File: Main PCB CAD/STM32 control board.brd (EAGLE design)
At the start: 130 x 100 mm, 118 parts, among them J1 PJ-063BH, J10 S3B-PH, J11 S3B-PH, J12 S3B-PH, J13 S3B-PH, J14 S6B-PH, J15 DG301-4P, J2 S3B-PH, J3 S4B-PH, J4 S6B-PH, J5 S3B-PH, J6 S10B-PH, J7 S10B-PH, J8 S10B-PH, J9 S10B-PH, SW1 B3F-4055, SW2 B3F-4055, SW3 B3F-4055, SW4 B3F-4055, SW5 B3F-4055, U1 STM32G474, U2 TPS7A19, U3 REF3330, U4 REF3318, U5 ICM_20600, U6 DRV8701VIA, U8 L2293Q, X1 CSTNE

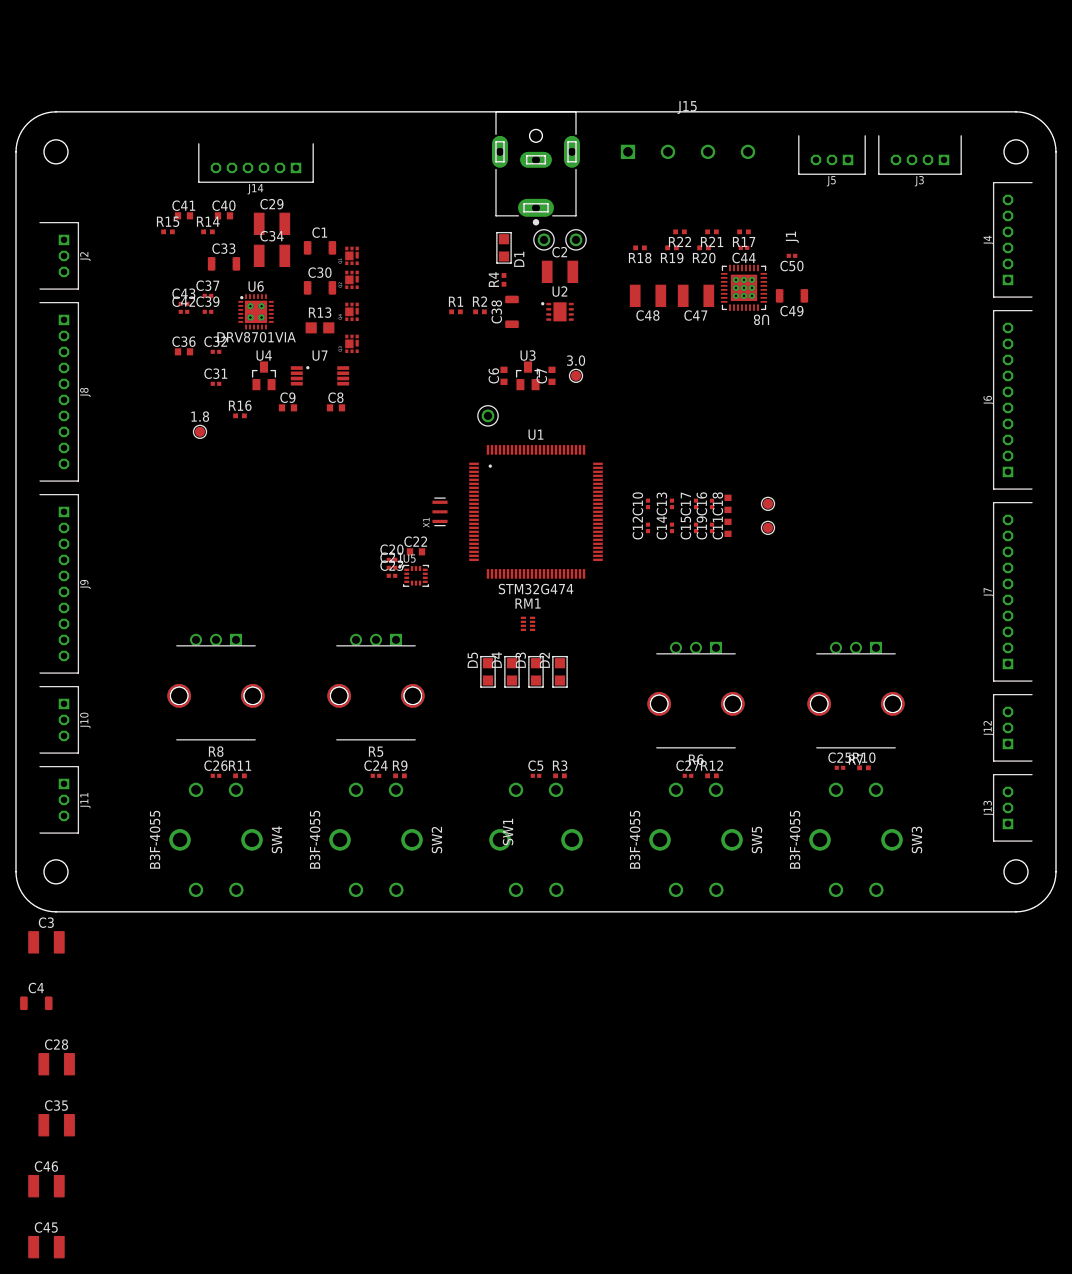
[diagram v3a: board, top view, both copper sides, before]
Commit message: components placement for review
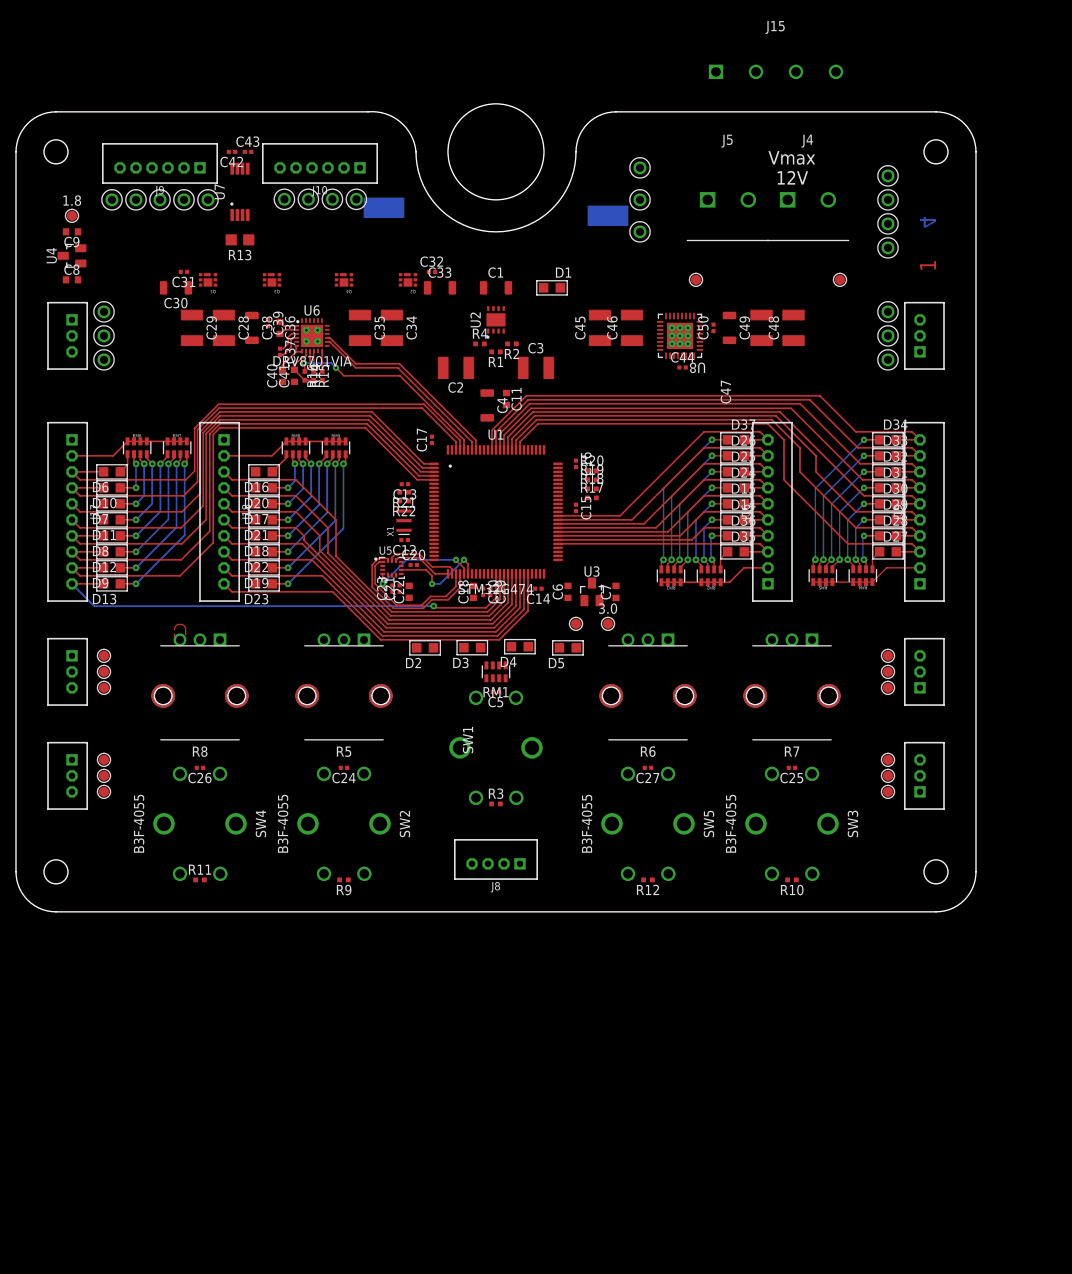
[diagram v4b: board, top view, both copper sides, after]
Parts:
- removed J1: PJ-063BH, commonly used connectors:CUI_PJ-063BH
- removed J11, J12, J13, J2: S3B-PH, con-jst-ph:S3B-PH-K
- removed J14: S6B-PH, con-jst-ph:S6B-PH-K
- removed J3: S4B-PH, con-jst-ph:S4B-PH-K
- added D10, D11, D12, D13, D14, D15, D16, D17, D18, D19, D20, D21, D22, D23, D24, D25, D26, D27, D28, D29, D30, D31, D32, D33, D34, D35, D36, D37, D6, D7, D8, D9: Blue, Semiconductor_devices:LED-0805
- added GND_, TP12, TP13, TP14, TP15, TP16, TP17, TP37, TP38, TP6, TP7, TP8, TP9: (no value), testing:TP1.27MM_MASK_SILKSCREEN
- added J16, J17, J18, J19: B10B-PH, con-jst-ph:B10B-PH-K
- added J20, J21, J22, J23: B3B-PH, con-jst-ph:B3B-PH-K
- added NEG, POS: (no value), testing:SMD_PAD
- added RM2, RM3, RM4, RM5, RM6, RM7, RM8, RM9: RES_ARRAY0603, Resistors:0603-ARC
- added TP18, TP19, TP20, TP21, TP22, TP23, TP24, TP25, TP26, TP27, TP28, TP29, TP30, TP31, TP32, TP33, TP34, TP35, TP36: (no value), testing:TEST_RING
- J10: value S3B-PH -> B6B-PH; device con-jst-ph:S3B-PH-K -> con-jst-ph:B6B-PH-K
- J4: value S6B-PH -> PC_1733570; device con-jst-ph:S6B-PH-K -> Terminal blocks:PC_1733570
- J5: value S3B-PH -> PC_1733570; device con-jst-ph:S3B-PH-K -> Terminal blocks:PC_1733570
- J6, J7: value S10B-PH -> B3B-PH; device con-jst-ph:S10B-PH-K -> con-jst-ph:B3B-PH-K
- J8: value S10B-PH -> B4B-PH; device con-jst-ph:S10B-PH-K -> con-jst-ph:B4B-PH-K
- J9: value S10B-PH -> B6B-PH; device con-jst-ph:S10B-PH-K -> con-jst-ph:B6B-PH-K
- RM1: value RES_ARRAY0402_YAGEO -> RES_ARRAY0603; device Resistors:0402-ARC -> Resistors:0603-ARC
- moved C45 134.1 mm to (73.0, 73.0), turned to 90 degrees
- moved C46 129.9 mm to (77.0, 73.0), turned to 90 degrees
- moved J7 121.3 mm to (7.00, 72.0), turned to 270 degrees
- moved C35 106.6 mm to (43.0, 73.0), turned to 270 degrees
- moved C28 94.4 mm to (26.0, 73.0), turned to 270 degrees
- moved C3 94.3 mm to (65.0, 68.0)
- moved C4 93.6 mm to (58.9, 63.3), turned to 270 degrees
- moved J8 80.0 mm to (60.0, 6.00), turned to 180 degrees
- moved J10 76.1 mm to (38.0, 93.0), turned to 180 degrees
- moved J9 53.4 mm to (18.0, 93.0), turned to 180 degrees
- moved R21 50.4 mm to (48.5, 52.5)
- moved R22 48.2 mm to (48.5, 51.4)
- moved R17 38.3 mm to (72.0, 51.7), turned to 0 degrees
- moved C8 36.7 mm to (7.00, 79.0)
- moved C9 34.8 mm to (7.00, 85.0), turned to 180 degrees
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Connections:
- removed net POUT1: J15.1, U8.31
- removed net POUT2: J15.2, U8.10
- removed net POUT3: J15.3, U8.16
- removed net POUT4: J15.4, U8.25
- new net N$10: D30.-, RM4.4
- new net N$12: D27.-, RM4.1
- new net N$13: D31.-, RM5.1
- new net N$14: D32.-, RM5.2
- new net N$22: D34.-, RM5.4
- new net N$23: D35.-, RM2.1
- new net N$25: D36.-, RM2.2
- new net N$26: D14.-, RM2.3
- new net N$27: D15.-, RM2.4
- new net N$28: D24.-, RM3.1
- new net N$29: D25.-, RM3.2
- new net N$3: D28.-, RM4.2
- new net N$30: D26.-, RM3.3
- new net N$31: D37.-, RM3.4
- new net N$34: D6.-, RM6.1
- new net N$35: D10.-, RM6.2
- new net N$36: D7.-, RM6.3
- new net N$38: D11.-, RM6.4
- new net N$39: D8.-, RM7.1
- new net N$40: D12.-, RM7.2
- new net N$41: D9.-, RM7.3
- new net N$42: D13.-, RM7.4
- new net N$43: D16.-, RM8.1
- new net N$44: D20.-, RM8.2
- new net N$45: D17.-, RM8.3
- new net N$46: D21.-, RM8.4
- new net N$47: D18.-, RM9.1
- new net N$48: D22.-, RM9.2
- new net N$49: D19.-, RM9.3
- new net N$50: D23.-, RM9.4
- new net N$9: D29.-, RM4.3
- new net PO1: J15.4, J5.2, TP33.1, U8.31
- new net PO2: J15.1, J5.1, TP34.1, U8.10
- new net PO3: J15.2, J4.2, TP35.1, U8.16
- new net PO4: J15.3, J4.1, TP36.1, U8.25
- net +3V: now also J20.1, J21.1, J22.1, J23.1, TP12.1, TP15.1, TP6.1, TP9.1
- net +3V3: now also C44.1, J10.2, J16.1, J17.1, J18.1, J19.1, U8.27; no longer J10.1, J11.1, J12.1, J13.1, J14.2, J3.1, J4.1, J6.1, J7.1
- net ENCODER_1: now also J10.3, TP30.1; no longer J14.3
- net ENCODER_2: now also J10.4, TP29.1; no longer J14.4
- net GND: now also GND_.1, J10.5, J16.2, J17.2, J18.2, J19.2, J20.3, J21.3, J22.3, J23.3, J6.3, J7.3, J8.4, J9.6, NEG.1, RM1.5, RM1.6, RM1.7, RM1.8, RM2.5, RM2.6, RM2.7, RM2.8, RM3.5, RM3.6, RM3.7, RM3.8, RM4.5, RM4.6, RM4.7, RM4.8, RM5.5, RM5.6, RM5.7, RM5.8, RM6.5, RM6.6, RM6.7, RM6.8, RM7.5, RM7.6, RM7.7, RM7.8, RM8.5, RM8.6, RM8.7, RM8.8, RM9.5, RM9.6, RM9.7, RM9.8, TP14.1, TP17.1, TP20.1, TP21.1, TP26.1, TP32.1, TP8.1; no longer D2.-, D3.-, D4.-, D5.-, J1.2, J1.S1, J1.S2, J10.3, J11.3, J12.3, J13.3, J14.5, J2.3, J3.4, J4.6, J5.3, J6.2, J7.2, J8.2, J9.2, TP10.1
- net I2C3_SCL: now also J6.2, TP27.1; no longer J5.2
- net I2C3_SDA: now also J6.1, TP28.1; no longer J5.1
- net M1: now also J10.1, TP31.1; no longer J14.1
- net M_SH2: now also J10.6; no longer J14.6
- net N$11: now also D5.-, RM1.4; no longer D2.+, RM1.11
- net N$17: now also D33.-, RM5.3; no longer C44.1, U8.27
- net N$19: now also TP37.1
- net N$20: now also TP38.1
- net N$4: now also D2.-, RM1.1; no longer D5.+, RM1.44
- net N$5: now also D3.-, RM1.2; no longer D4.+, RM1.33
- net N$6: now also D4.-, RM1.3; no longer D3.+, RM1.22
- net PA0: now also J20.2, TP7.1; no longer J10.2
- net PA1: now also J21.2, TP10.1; no longer J11.2
- net PA2: now also J22.2, TP13.1; no longer J12.2
- net PA3: now also J23.2, TP16.1; no longer J13.2
- net PB1: now also D4.+; no longer RM1.3
- net PB2: now also D5.+; no longer RM1.4
- net PC6: now also D2.+; no longer RM1.1
- net PC7: now also D3.+; no longer RM1.2
- net PD0: now also D27.+, J19.3; no longer J6.3
- net PD1: now also D28.+, J19.4; no longer J6.4
- net PD10: now also D14.+, J16.5; no longer J7.5
- net PD11: now also D15.+, J16.6; no longer J7.6
- net PD12: now also D24.+, J16.7; no longer J7.7
- net PD13: now also D25.+, J16.8; no longer J7.8
- net PD14: now also D26.+, J16.9; no longer J7.9
- net PD15: now also D37.+, J16.10; no longer J7.10
- net PD2: now also D29.+, J19.5; no longer J6.5
- net PD3: now also D30.+, J19.6; no longer J6.6
- net PD4: now also D31.+, J19.7; no longer J6.7
- net PD5: now also D32.+, J19.8; no longer J6.8
- net PD6: now also D33.+, J19.9; no longer J6.9
- net PD7: now also D34.+, J19.10; no longer J6.10
- net PD8: now also D35.+, J16.3; no longer J7.3
- net PD9: now also D36.+, J16.4; no longer J7.4
- net PE0: now also D6.+, J17.3; no longer J8.3
- net PE1: now also D10.+, J17.4; no longer J8.4
- net PE10: now also D17.+, J18.5; no longer J9.5
- net PE11: now also D21.+, J18.6; no longer J9.6
- net PE12: now also D18.+, J18.7; no longer J9.7
- net PE13: now also D22.+, J18.8; no longer J9.8
- net PE14: now also D19.+, J18.9; no longer J9.9
- net PE15: now also D23.+, J18.10; no longer J9.10
- net PE2: now also D7.+, J17.5; no longer J8.5
- net PE3: now also D11.+, J17.6; no longer J8.6
- net PE4: now also D8.+, J17.7; no longer J8.7
- net PE5: now also D12.+, J17.8; no longer J8.8
- net PE6: now also D9.+, J17.9; no longer J8.9
- net PE7: now also D13.+, J17.10; no longer J8.10
- net PE8: now also D16.+, J18.3; no longer J9.3
- net PE9: now also D20.+, J18.4; no longer J9.4
- net SPI3_MISO: now also J9.3, TP24.1; no longer J4.3
- net SPI3_MOSI: now also J9.2, TP25.1; no longer J4.2
- net SPI3_SCK: now also J9.4, TP23.1; no longer J4.4
- net SPI_CS: now also J9.5, TP22.1; no longer J4.5
- net SWCLK: now also J8.3; no longer J3.3
- net SWDIO: now also J8.2; no longer J3.2
- net USART3_RX: now also J7.2, TP19.1; no longer J2.2
- net USART3_TX: now also J7.1, TP18.1; no longer J2.1
- net VDD: now also POS.1; no longer J1.1
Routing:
- net PE6: track 0.00 -> 67.9 mm
- net PE5: track 0.00 -> 66.5 mm
- net PE4: track 0.00 -> 65.0 mm
- net PD0: track 0.00 -> 64.4 mm
- net PE1: track 0.00 -> 63.5 mm
- net PD1: track 0.00 -> 63.5 mm
- net PD2: track 0.00 -> 63.1 mm
- net PE0: track 0.00 -> 63.0 mm
- net PD7: track 0.00 -> 63.0 mm
- net PD6: track 0.00 -> 62.8 mm
- net PD5: track 0.00 -> 62.5 mm
- net PD4: track 0.00 -> 62.3 mm
- net PD3: track 0.00 -> 62.1 mm
- net PE7: track 0.00 -> 61.7 mm, vias 0 -> 1
- net PE3: track 0.00 -> 59.5 mm
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- added copper zone on layer 1, net GND
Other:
- board size 130 x 100 mm -> 120 x 100 mm
- board text added: "1"
- board text added: "2"
- board text added: "3"
- board text added: "4"
- board text added: "Vmax 12V"
